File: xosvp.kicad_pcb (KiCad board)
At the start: 2 copper layers, 49.5 x 50 mm, 14 parts

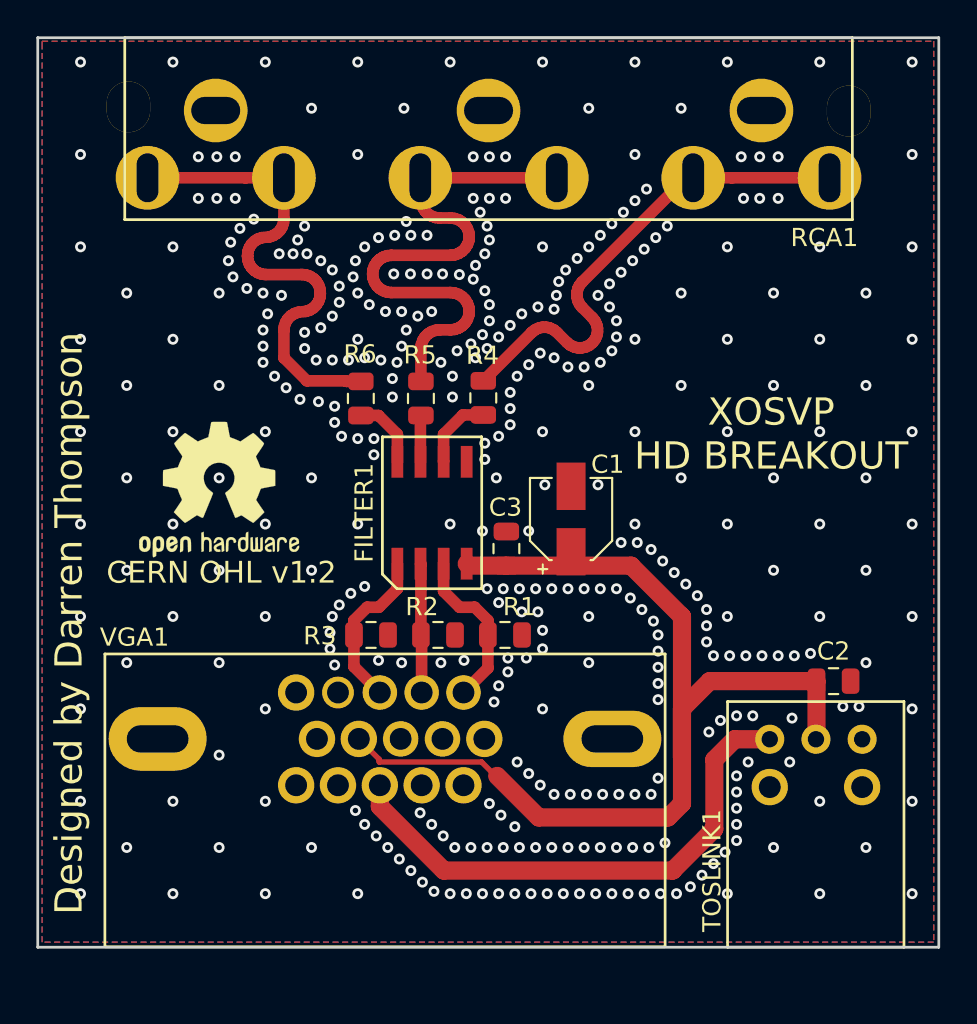
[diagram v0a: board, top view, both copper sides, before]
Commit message: pcb changes
- toslink footprint variation
- connector labeling
- round edges
- schematic header
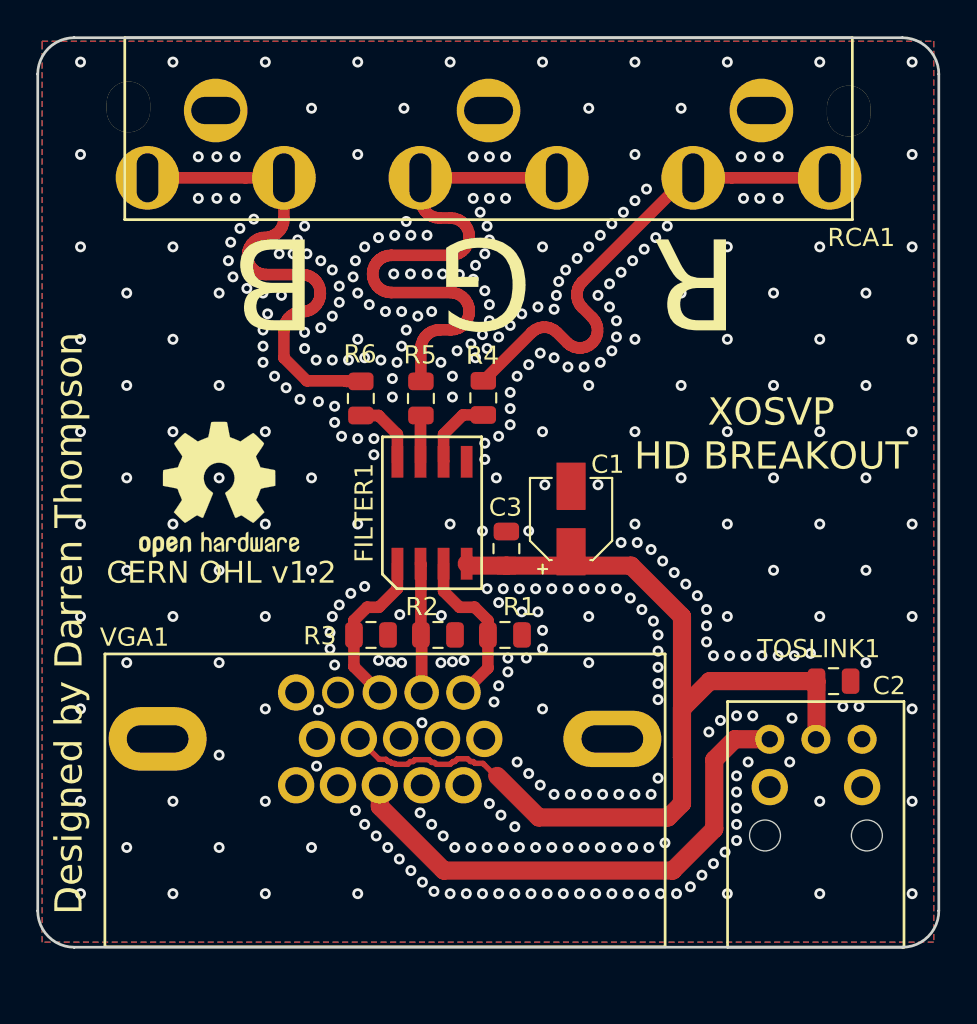
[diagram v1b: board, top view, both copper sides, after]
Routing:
- net +5V: track 57.2 -> 61.2 mm
- net Earth: vias 373 -> 378
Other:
- outline, holes or cut-outs redrawn
- board text added: "2020"
- board text added: "R G B"
- board text added: "https://www.designer2k2.at"
